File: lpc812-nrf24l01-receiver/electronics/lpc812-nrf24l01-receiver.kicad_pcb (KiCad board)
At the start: 2 copper layers, 25 x 29 mm, 21 parts, among them K1 BAT, K2 CH3, K3 TH, K4 ST, P1 NRF24L01+, SW1 BIND/ISP, U1 MCP1703, U2 LPC812, X1 16MHz

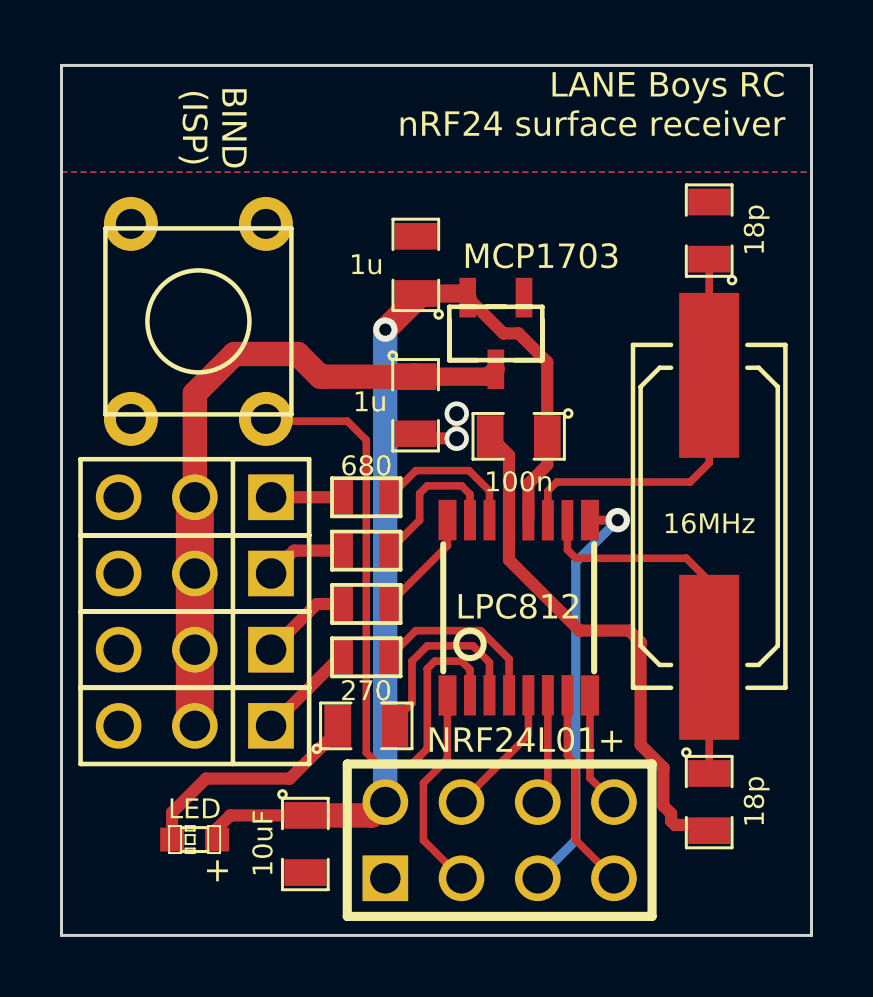
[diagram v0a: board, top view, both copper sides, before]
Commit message: Add 100uF cap against brown-out, add pull-down to prevent floating MISO
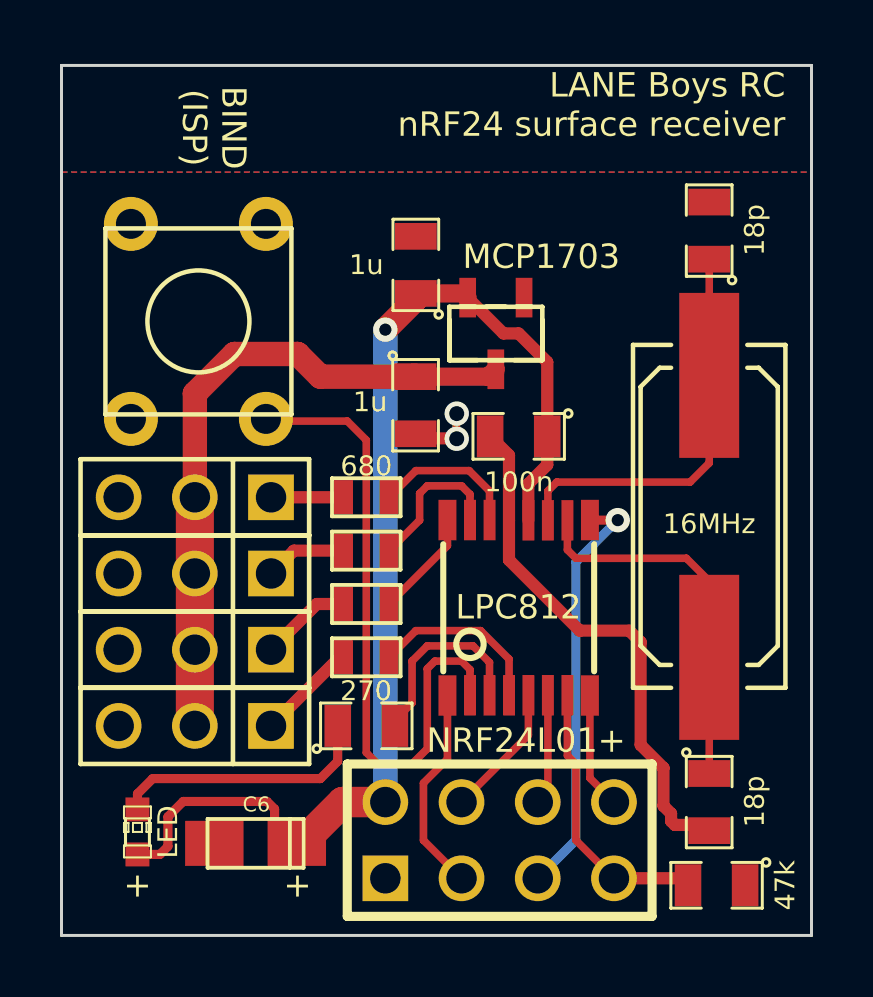
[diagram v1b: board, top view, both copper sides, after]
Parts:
- added R6: 47k, SM0805, F.Cu at (84.8, 84.3)
- C6: value 10uF -> 100uF; footprint SM0805 -> c_tant_A
- moved D1 1.92 mm to (65.5, 82.5), turned to 90 degrees
- moved C6 1.66 mm to (69.5, 82.9), turned to 0 degrees
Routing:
- net +3.3V: track 34.6 -> 39.2 mm
- net /MISO: track 6.74 -> 9.31 mm
- net N-000002: track 7.81 -> 8.82 mm
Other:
- board text added: "Rev 2"
- board text removed: "Rev 1"
